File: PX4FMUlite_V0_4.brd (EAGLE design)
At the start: 48.6 x 34.9 mm, 132 parts, among them J2 DF13-4P-1.25V, J201 DF13C-6P-1.25V, J202 DF13C-6P-1.25V, J203 DF13C-6P-1.25V, J3 DF13C-4P-1.25V, J302 DF13C-4P-1.25V, J401 DF13C-4P-1.25V, J403 DF13C-7P-1.25V, J405 DF13C-4P-1.25V, J802 DF13C-3P-1.25V, M3_MOUNT1101 MOUNT-HOLE3.1MM, M3_MOUNT1102 MOUNT-HOLE3.1MM, M3_MOUNT1103 MOUNT-HOLE3.1MM, M3_MOUNT1104 MOUNT-HOLE3.1MM, U101 STM32F4X7VX, U2 MAX3051, U401 MAX3051, X101 3.2x2.5 mm / 24 MHz / 15 ppm

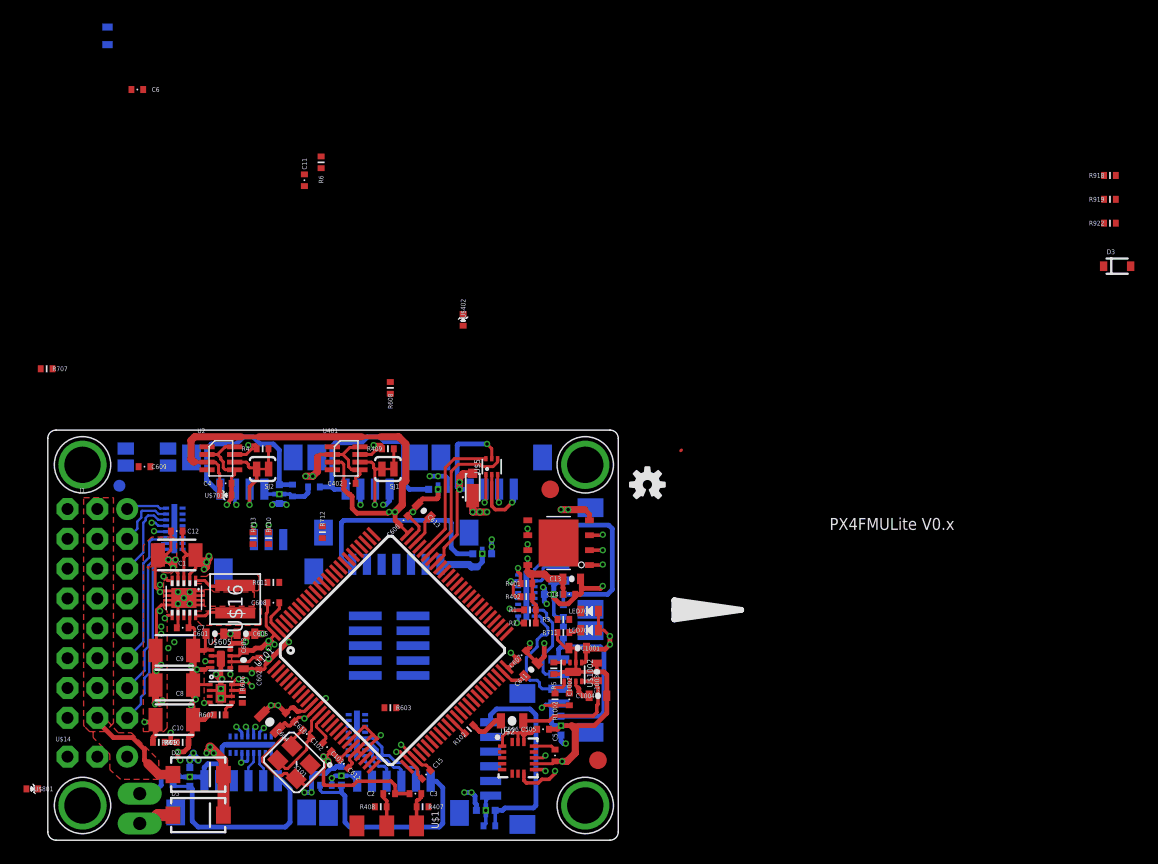
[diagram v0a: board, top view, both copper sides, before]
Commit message: Blue LED removed
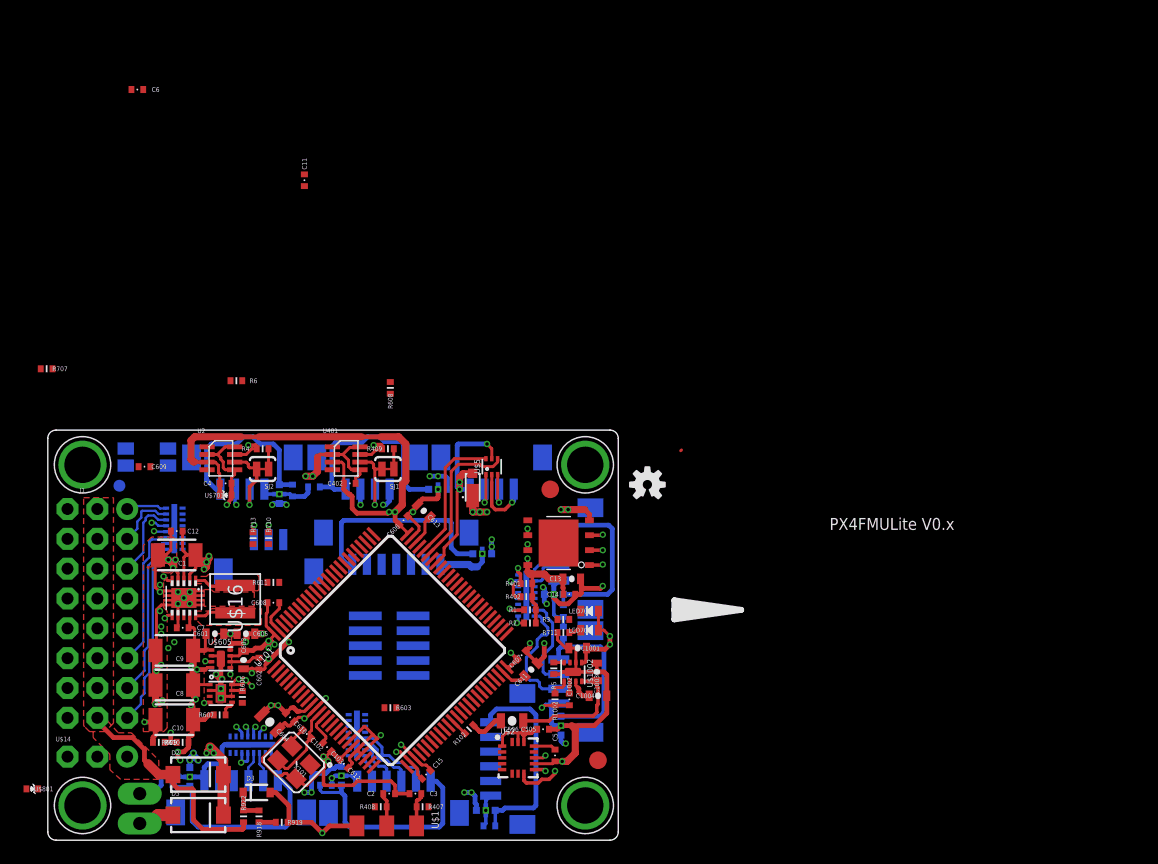
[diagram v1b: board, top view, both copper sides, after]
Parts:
- removed LED705: BLUE, pixhawk2:0603-LED
- removed R712: 220R, pixhawk2:0402-RES
- removed U$402: PESD0402-140, pixhawk2:0402-TVS
- moved R918 90.7 mm to (27.2, 4.78), turned to 90 degrees
- moved R922 89.4 mm to (25.9, 4.78), turned to 270 degrees
- moved R919 88.2 mm to (29.2, 4.27), turned to 180 degrees
- moved D3 85.9 mm to (27.0, 6.81)
- moved R6 19.9 mm to (25.3, 41.9), turned to 180 degrees
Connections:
- removed net FMU-LED_BLUE: R712.P$1
- removed net N$9: LED705.C, R712.P$2
- net GND: no longer U$402.A
- net N$41: no longer U$402.C
- net VDD_5V: no longer LED705.A
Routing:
- net V_SERVO: track 9.15 -> 19.6 mm
- net GND: track 193.5 -> 203.6 mm, vias 38 -> 39
- net N$6: track 0.00 -> 2.87 mm
- net VDD_SERVO_SENS: track 0.00 -> 1.43 mm

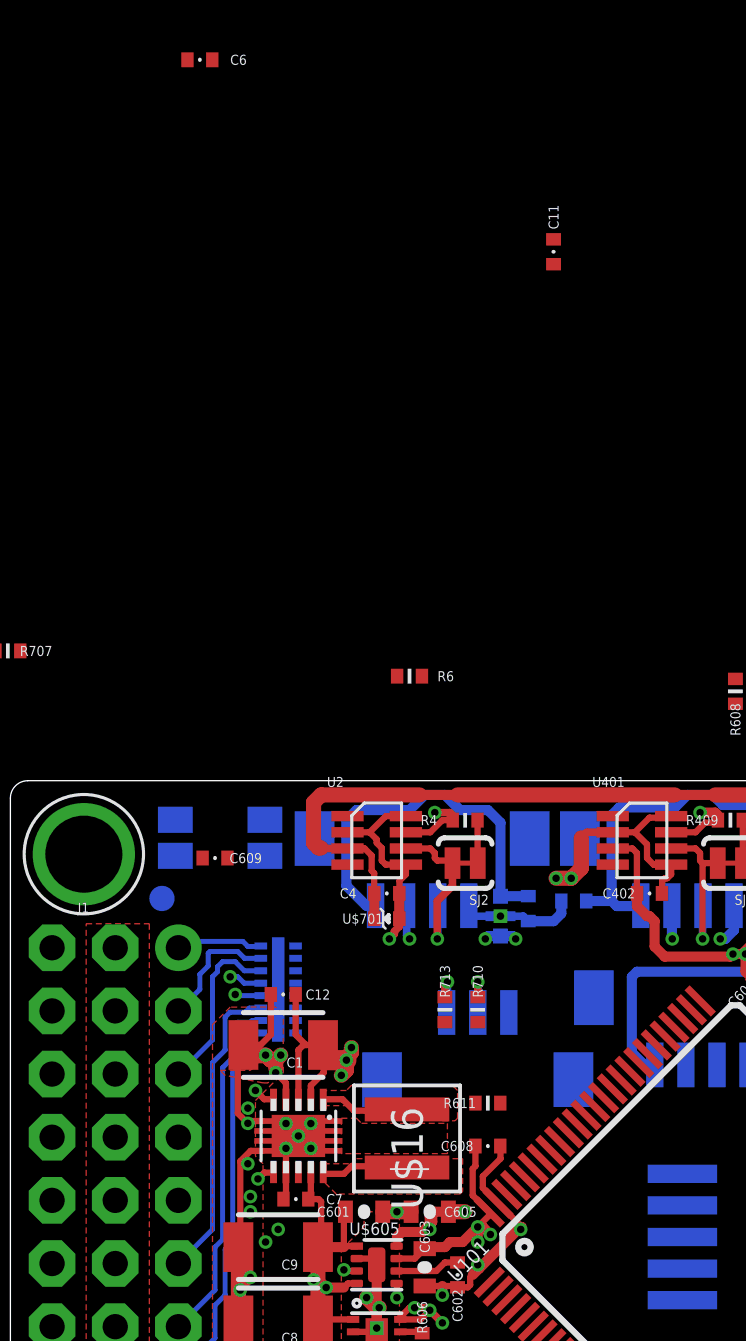
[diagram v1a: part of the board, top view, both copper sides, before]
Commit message: Positioned buckboost Vaux decoupling cap
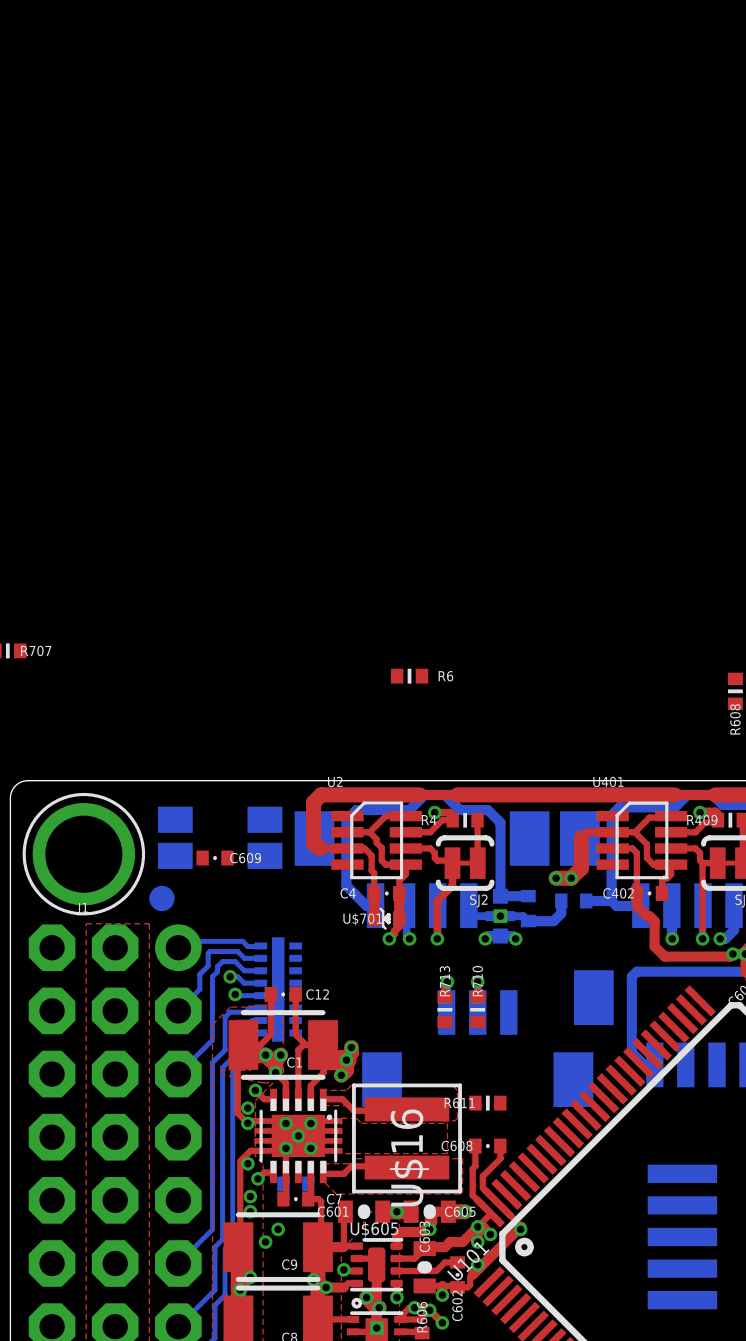
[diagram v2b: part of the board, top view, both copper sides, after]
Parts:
- removed C11: 0u1, pixhawk2:0402-CAP
- moved C6 45.4 mm to (20.7, 21.4), flipped to the bottom
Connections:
- net GND: no longer C11.P$2
- net VDD_5V: no longer C11.P$1

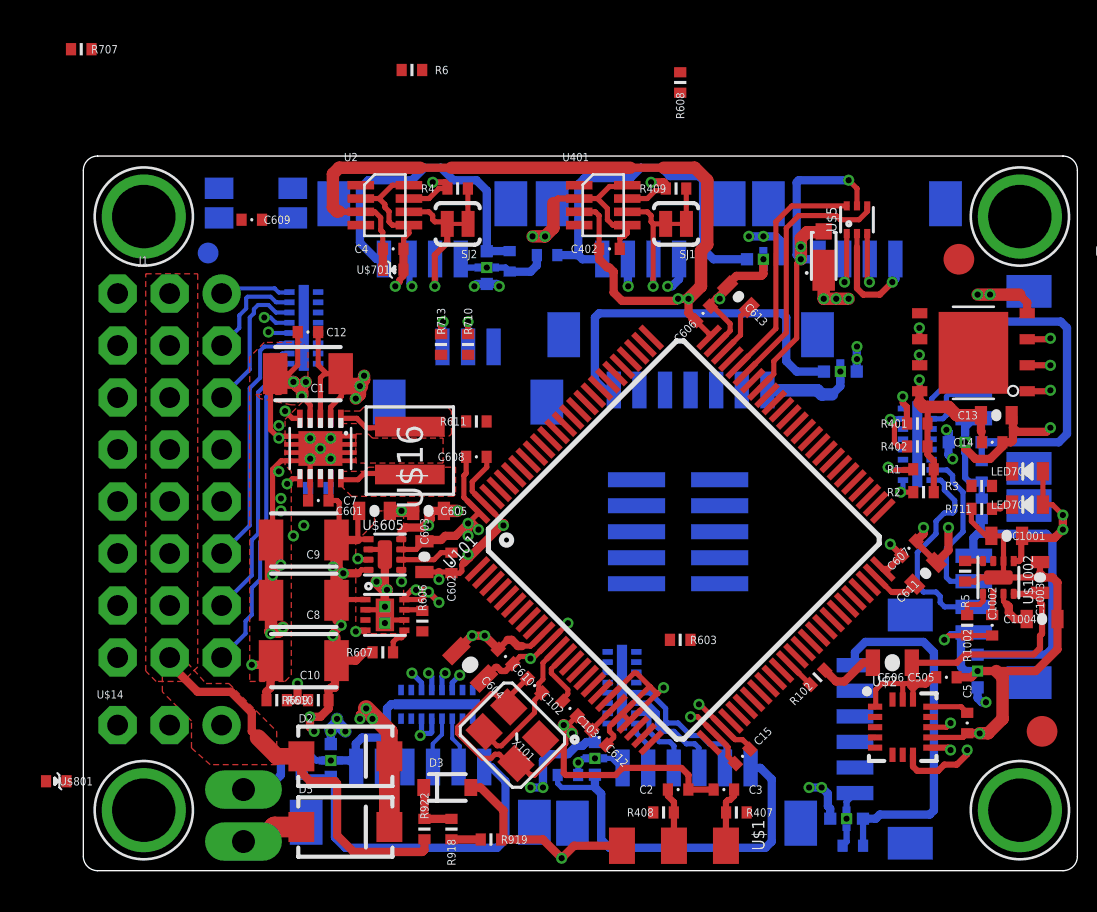
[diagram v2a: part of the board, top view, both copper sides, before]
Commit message: Everything fitted before autoroute
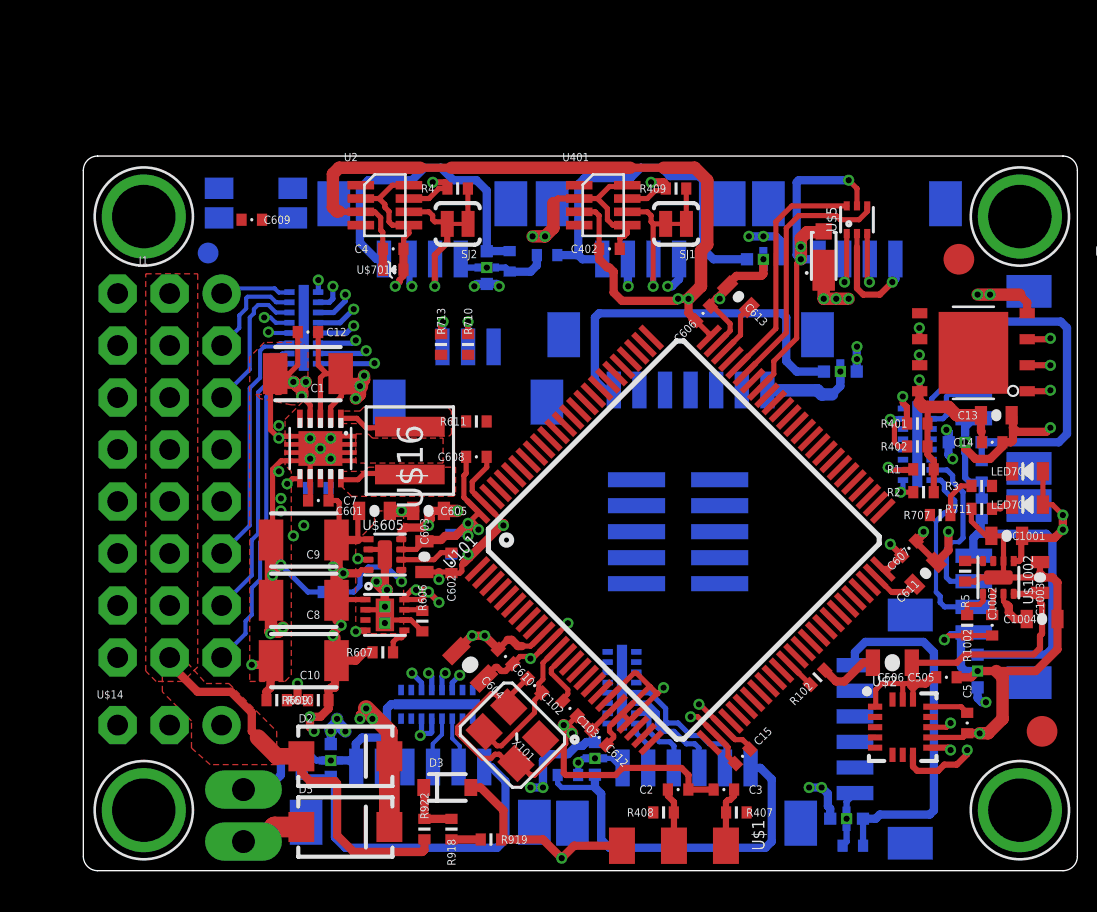
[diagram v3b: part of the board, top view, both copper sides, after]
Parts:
- removed R6: 10K, pixhawk2:0402-RES
- removed U$801: PESD0402-140, pixhawk2:0402-TVS
- moved R707 47.7 mm to (51.1, 20.1), turned to 0 degrees
- moved R608 25.2 mm to (27.2, 18.7), flipped to the bottom
- moved R603 17.1 mm to (21.4, 16.4), flipped to the bottom
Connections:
- removed net !VDD_5V_VALID: R6.P$1, U$15.5, U101.91
- new net !EX_VDD_5V_VALID: U101.91
- net GND: no longer U$801.A
- net VDD_3V3_SPEKTRUM: no longer U$801.C
- net VDD_5V: no longer R6.P$2
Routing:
- net VDD_3V3_SPEKTRUM_EN: track 0.58 -> 4.53 mm
- net GND: track 203.6 -> 206.8 mm
- net FMU-CH8: track 0.00 -> 2.76 mm, vias 0 -> 1
- net FMU-CH7: track 0.00 -> 2.40 mm, vias 0 -> 1
- net N$13: track 0.00 -> 2.15 mm
- net FMU-CH4: track 0.00 -> 2.01 mm, vias 0 -> 1
- net FMU-CH6: track 0.00 -> 1.90 mm, vias 0 -> 1
- net FMU-CH5: track 0.00 -> 1.88 mm, vias 0 -> 1
- net FMU-CH3: track 0.00 -> 1.87 mm, vias 0 -> 1
- net FMU-CH2: track 0.00 -> 1.40 mm, vias 0 -> 1
- net !VDD_5V_VALID: track 1.16 -> 0.00 mm, vias 1 -> 0
- net N$20: track 10.3 -> 9.14 mm
- net FMU-VDD_3V3: track 83.7 -> 84.6 mm
- net FMU-CH1: track 0.00 -> 0.60 mm, vias 0 -> 1
